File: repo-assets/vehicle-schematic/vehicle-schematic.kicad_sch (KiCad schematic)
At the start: 6 parts, among them U1 Peripherals Interface Board, U2 Raspberry Pi 5, U3 Pi Camera 3, U4 N20 Motor With Encoder, U5 TFLuna 1D LiDAR

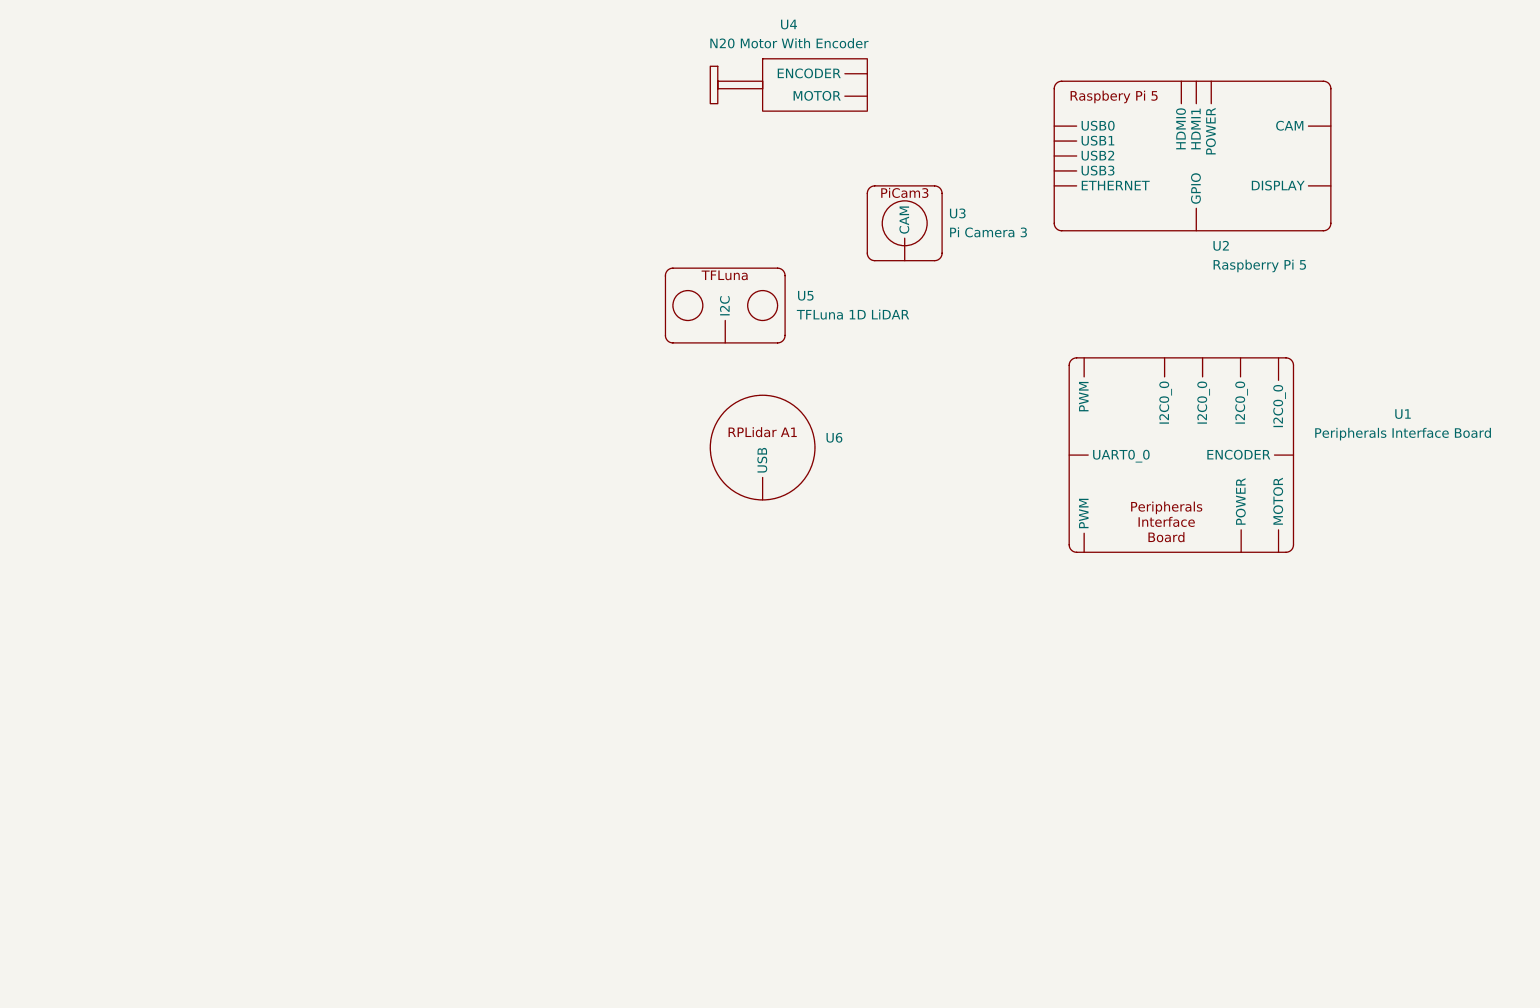
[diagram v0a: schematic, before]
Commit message: Create temporary symbols and layout for vehicle wiring schematic
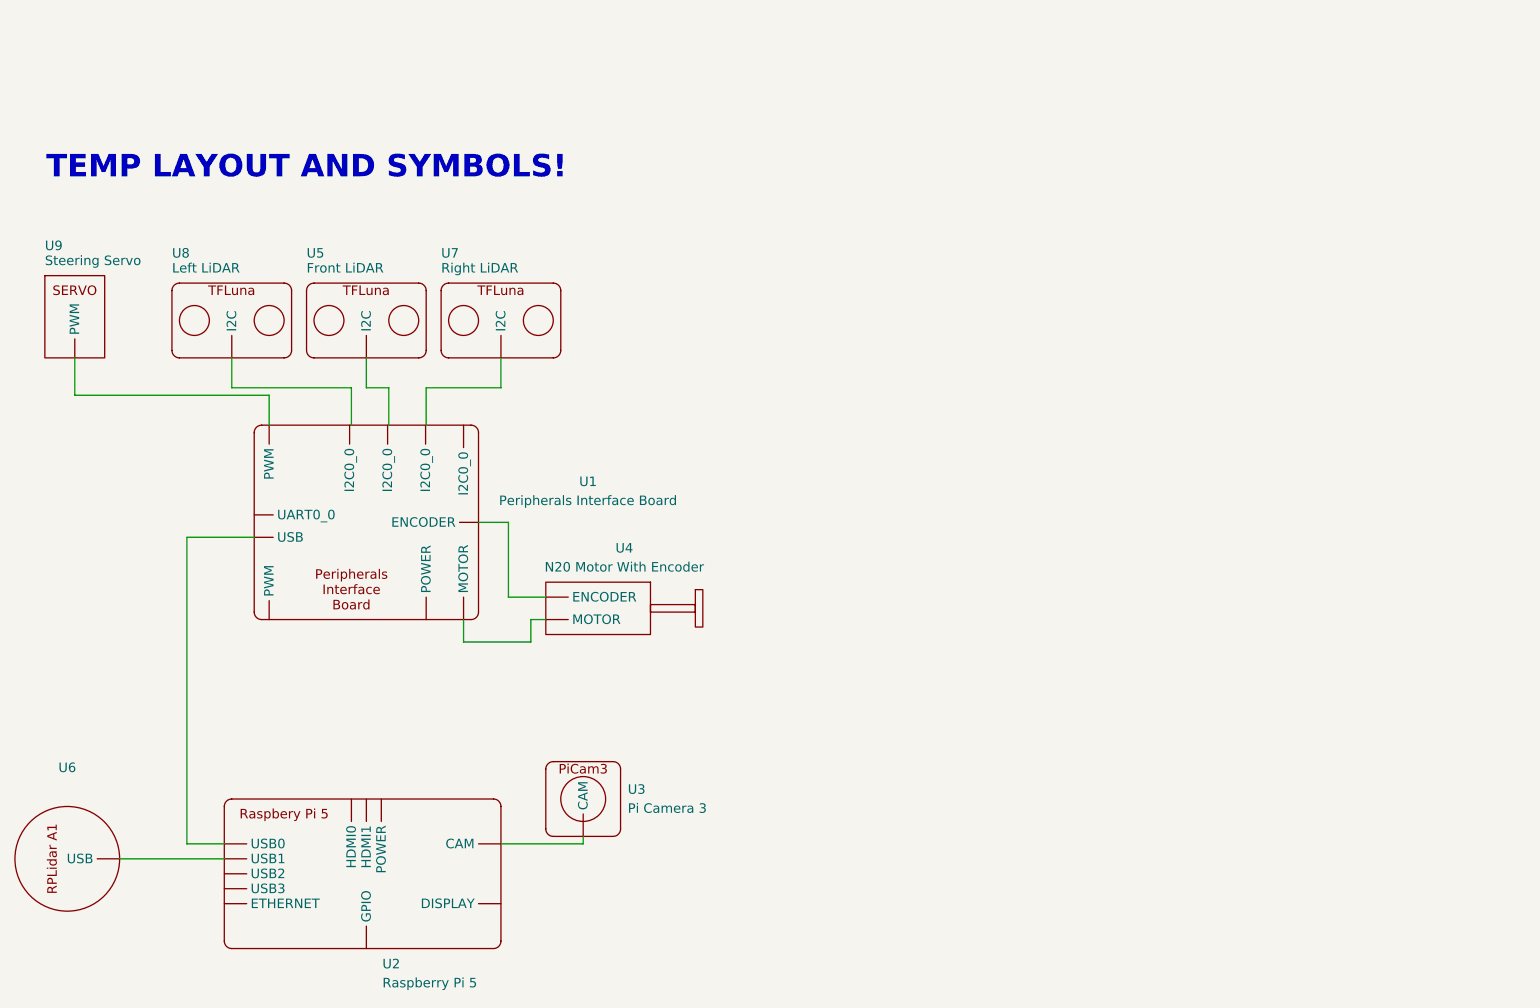
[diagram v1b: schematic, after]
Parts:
- added U7: Right LiDAR, symbol bot-symbols:LiDAR
- added U8: Left LiDAR, symbol bot-symbols:LiDAR
- added U9: Steering Servo, symbol bot-symbols:Servo
- U5: value TFLuna 1D LiDAR -> Front LiDAR
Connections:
- net at U4. (MOTOR): now also U1. (ENCODER)
- net at U3. (CAM): now also U2. (DISPLAY)
- net at U2. (DISPLAY): now also U6. (USB)
- new net: U1. (ENCODER), U9. (PWM)
- new net: U1. (ENCODER), U4. (MOTOR)
- new net: U1. (ENCODER), U2. (DISPLAY)
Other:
- note added: "TEMP LAYOUT AND SYMBOLS!"
- moved on the sheet: U2, U3, U4, U5, U6
